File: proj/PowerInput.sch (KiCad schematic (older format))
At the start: 23 parts, among them Q1 MMBT3906, Q2 IRLML6402, U1 TL431AIDBZ, U2 LM393M

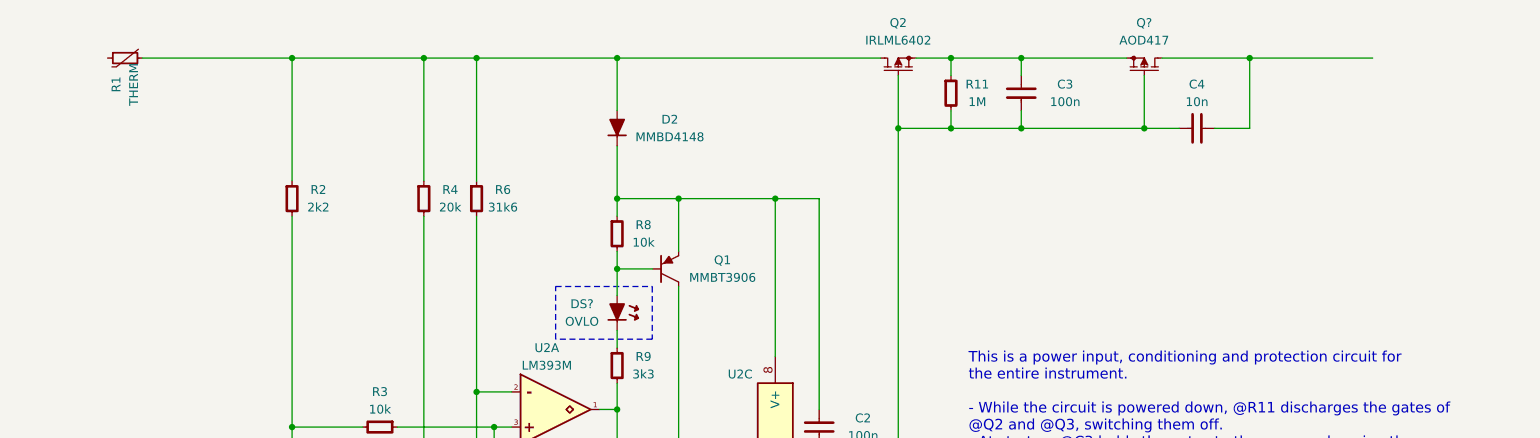
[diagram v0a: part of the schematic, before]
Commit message: Add DC-DC
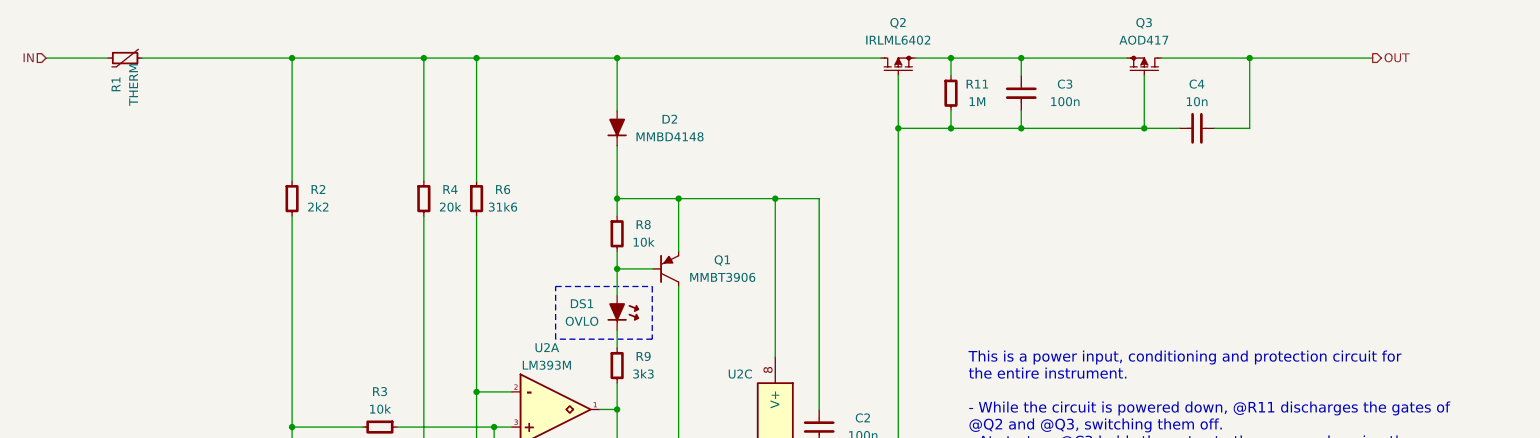
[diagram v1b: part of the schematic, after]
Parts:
- gave numbers to parts that had none: 2
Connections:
- net IN: now reaches R1.1
- net OUT: now reaches C4.1, Q3.3 (D)
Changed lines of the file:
@@
 $Descr USLegal 14000 8500
 encoding utf-8
-Sheet 3 13
+Sheet 3 14
 Title ""
 Date ""
@@
 Connection ~ 4450 5100
 $Comp
-L GND #PWR1
+L GND #PWR2
 U 1 1 54F4C586
 P 4450 6050
-F 0 "#PWR1" H 4450 6050 30  0001 C CNN
+F 0 "#PWR2" H 4450 6050 30  0001 C CNN
 F 1 "GND" H 4450 5980 30  0001 C CNN
 F 2 "" H 4450 6050 60  0000 C CNN
@@
 $EndComp
 $Comp
-L GND #PWR2
+L GND #PWR3
 U 1 1 54F4C600
 P 5200 6000
-F 0 "#PWR2" H 5200 6000 30  0001 C CNN
+F 0 "#PWR3" H 5200 6000 30  0001 C CNN
 F 1 "GND" H 5200 5930 30  0001 C CNN
 F 2 "" H 5200 6000 60  0000 C CNN
@@
 	5200 6000 5200 5900
 $Comp
-L GND #PWR3
+L GND #PWR4
 U 1 1 54F4C674
 P 5500 6000
-F 0 "#PWR3" H 5500 6000 30  0001 C CNN
+F 0 "#PWR4" H 5500 6000 30  0001 C CNN
 F 1 "GND" H 5500 5930 30  0001 C CNN
 F 2 "" H 5500 6000 60  0000 C CNN
@@
 Connection ~ 7200 2900
 $Comp
-L GND #PWR6
+L GND #PWR7
 U 1 1 54F4D4FF
 P 7450 4400
-F 0 "#PWR6" H 7450 4400 30  0001 C CNN
+F 0 "#PWR7" H 7450 4400 30  0001 C CNN
 F 1 "GND" H 7450 4330 30  0001 C CNN
 F 2 "" H 7450 4400 60  0000 C CNN
@@
 	7450 4400 7450 4300
 $Comp
-L GND #PWR5
+L GND #PWR6
 U 1 1 54F4D5D3
 P 7200 4700
-F 0 "#PWR5" H 7200 4700 30  0001 C CNN
+F 0 "#PWR6" H 7200 4700 30  0001 C CNN
 F 1 "GND" H 7200 4630 30  0001 C CNN
 F 2 "" H 7200 4700 60  0000 C CNN
@@
 Connection ~ 5500 5600
 $Comp
-L GND #PWR4
+L GND #PWR5
 U 1 1 54F4E909
 P 5850 6000
-F 0 "#PWR4" H 5850 6000 30  0001 C CNN
+F 0 "#PWR5" H 5850 6000 30  0001 C CNN
 F 1 "GND" H 5850 5930 30  0001 C CNN
 F 2 "" H 5850 6000 60  0000 C CNN
@@
 $EndComp
 $Comp
-L AOD417 Q?
+L AOD417 Q3
 U 1 1 54F5B784
 P 9300 2150
-F 0 "Q?" V 9550 2150 50  0000 C CNN
+F 0 "Q3" V 9550 2150 50  0000 C CNN
 F 1 "AOD417" V 9450 2150 50  0000 C CNN
 F 2 "smd-semi:TO-252" H 9450 2100 50  0001 C CNN
@@
 $EndComp
 $Comp
-L LED-0603 DS?
+L LED-0603 DS1
 U 1 1 54F5C5AB
 P 6300 3550
-F 0 "DS?" H 6100 3600 50  0000 C CNN
+F 0 "DS1" H 6100 3600 50  0000 C CNN
 F 1 "OVLO" H 6100 3500 50  0000 C CNN
 F 2 "smd-semi:LED-0603" H 6300 3550 50  0001 C CNN
@@
 	1    0    0    -1
 $EndComp
+Text HLabel 10600 2100 2    50   Output ~ 0
+OUT
+Text HLabel 3050 2100 0    50   Input ~ 0
+IN
+Wire Wire Line
+	3050 2100 3400 2100
 $EndSCHEMATC

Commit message: Finish USB subcircuit
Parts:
- added Q?: MMBT3904, smd-semi:SOT-23, symbol MMBT3904
- added R? (x2): 10k, IPC7351-Nominal:RESC1005X40, symbol R-0402
- R1: value THERM -> 350mA; footprint (none) -> IPC7351-Nominal:RESC3216X60; BOM (none) -> DIST DIGIKEY 507-1801-1-ND; Manuf (none) -> BelFuse; PN (none) -> 0ZCJ0035AF2E
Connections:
- net GND: now also Q?.2, R?.2
- net at R4.2, R5.1, U2.6: now also Q?.3
- new net: Q?.1, R?.1, R?.1
- new net PWRDN: R?.2
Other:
- moved on the sheet: C2, C3, C4, Q2, Q3, R11, R2, U1, U2C

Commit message: Start PCB
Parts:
- gave numbers to parts that had none: 3
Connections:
- net GND: no longer R2.2, R3.2, U1.2, U2.5
- net at U1.1: now also R2.2, R3.2, U1.2, U2.5
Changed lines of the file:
@@
 $EndComp
 Wire Wire Line
-	3600 2100 4100 2100
-Wire Wire Line
-	4100 2100 5200 2100
-Wire Wire Line
-	5200 2100 5500 2100
-Wire Wire Line
-	5500 2100 6300 2100
-Wire Wire Line
-	6300 2100 8300 2100
-Wire Wire Line
-	8500 2100 8700 2100
-Wire Wire Line
-	8700 2100 9100 2100
-Wire Wire Line
-	9100 2100 9700 2100
-Wire Wire Line
-	8400 5000 8400 2500
-Wire Wire Line
-	8400 2500 8400 2200
-Wire Wire Line
-	8400 2500 8700 2500
-Wire Wire Line
-	8700 2500 9100 2500
-Wire Wire Line
-	9100 2500 9800 2500
-Wire Wire Line
-	9800 2500 10000 2500
+	3600 2100 8300 2100
+Wire Wire Line
+	8500 2100 9700 2100
+Wire Wire Line
+	8400 5000 8400 2200
+Wire Wire Line
+	8400 2500 10000 2500
 Wire Wire Line
 	9800 2500 9800 2200
 Wire Wire Line
-	9900 2100 10400 2100
-Wire Wire Line
-	10400 2100 11100 2100
+	9900 2100 11100 2100
 $Comp
 L R-0402 R11
@@
 $EndComp
 Wire Wire Line
-	6300 3950 6300 4100
-Wire Wire Line
-	6300 4100 6300 4500
+	6300 3950 6300 4500
 Wire Wire Line
 	6300 4100 6200 4100
@@
 $EndComp
 Wire Wire Line
-	6300 3200 6300 3300
-Wire Wire Line
-	6300 3300 6300 3450
+	6300 3200 6300 3450
 $Comp
 L MMBT3906 Q1
@@
 	6650 3400 6650 5000
 Wire Wire Line
-	6550 5000 6650 5000
-Wire Wire Line
-	6650 5000 8400 5000
+	6550 5000 8400 5000
 Wire Wire Line
 	6650 3200 6650 2900
 Wire Wire Line
-	6300 2600 6300 2900
-Wire Wire Line
-	6300 2900 6300 3000
+	6300 2600 6300 3000
 $Comp
 L MMBD4148 D1
@@
 	5600 4500 5600 4200
 Wire Wire Line
-	5050 4200 5600 4200
-Wire Wire Line
-	5600 4200 5700 4200
+	5050 4200 5700 4200
 $Comp
 L R-0402 R3
@@
 $EndComp
 Wire Wire Line
-	5200 3000 5200 4900
-Wire Wire Line
-	5200 4900 5200 5300
-Wire Wire Line
-	5200 5300 5200 5700
+	5200 3000 5200 5700
 Wire Wire Line
 	5200 4900 5700 4900
@@
 $EndComp
 Wire Wire Line
-	5500 3000 5500 4000
-Wire Wire Line
-	5500 4000 5500 5600
-Wire Wire Line
-	5500 5600 5500 5700
+	5500 3000 5500 5700
 Wire Wire Line
 	5500 4000 5700 4000
@@
 	4100 5100 5700 5100
 Wire Wire Line
-	4100 3000 4100 4200
-Wire Wire Line
-	4100 4200 4100 5100
-Wire Wire Line
-	4100 5100 4100 5600
-Wire Wire Line
-	4100 5600 4100 5950
-Wire Wire Line
-	4100 5950 4100 6050
-Wire Wire Line
 	4100 4200 4850 4200
 $Comp
@@
 Connection ~ 4100 5100
 $Comp
-L GND #PWR2
+L GND #PWR0209
 U 1 1 54F4C586
 P 4100 6050
-F 0 "#PWR2" H 4100 6050 30  0001 C CNN
+F 0 "#PWR0209" H 4100 6050 30  0001 C CNN
 F 1 "GND" H 4100 5980 30  0001 C CNN
 F 2 "" H 4100 6050 60  0000 C CNN
@@
 $EndComp
 $Comp
-L GND #PWR3
+L GND #PWR0210
 U 1 1 54F4C600
 P 5200 6000
-F 0 "#PWR3" H 5200 6000 30  0001 C CNN
+F 0 "#PWR0210" H 5200 6000 30  0001 C CNN
 F 1 "GND" H 5200 5930 30  0001 C CNN
 F 2 "" H 5200 6000 60  0000 C CNN
@@
 	5200 6000 5200 5900
 $Comp
-L GND #PWR4
+L GND #PWR0211
 U 1 1 54F4C674
 P 5500 6000
-F 0 "#PWR4" H 5500 6000 30  0001 C CNN
+F 0 "#PWR0211" H 5500 6000 30  0001 C CNN
 F 1 "GND" H 5500 5930 30  0001 C CNN
 F 2 "" H 5500 6000 60  0000 C CNN
@@
 Connection ~ 7300 2900
 $Comp
-L GND #PWR7
+L GND #PWR0212
 U 1 1 54F4D4FF
 P 7550 4400
-F 0 "#PWR7" H 7550 4400 30  0001 C CNN
+F 0 "#PWR0212" H 7550 4400 30  0001 C CNN
 F 1 "GND" H 7550 4330 30  0001 C CNN
 F 2 "" H 7550 4400 60  0000 C CNN
@@
 	7550 4400 7550 4300
 $Comp
-L GND #PWR6
+L GND #PWR0213
 U 1 1 54F4D5D3
 P 7300 4700
-F 0 "#PWR6" H 7300 4700 30  0001 C CNN
+F 0 "#PWR0213" H 7300 4700 30  0001 C CNN
 F 1 "GND" H 7300 4630 30  0001 C CNN
 F 2 "" H 7300 4700 60  0000 C CNN
@@
 Connection ~ 5500 5600
 $Comp
-L GND #PWR5
+L GND #PWR0214
 U 1 1 54F4E909
 P 5850 6000
-F 0 "#PWR5" H 5850 6000 30  0001 C CNN
+F 0 "#PWR0214" H 5850 6000 30  0001 C CNN
 F 1 "GND" H 5850 5930 30  0001 C CNN
 F 2 "" H 5850 6000 60  0000 C CNN
@@
 Wire Notes Line
 	5950 3700 5950 3400
-Connection ~ 4100 5950
 $Comp
 L IRLML6402 Q2
@@
 	3050 2100 3400 2100
 $Comp
-L MMBT3904 Q?
+L MMBT3904 Q14
 U 1 1 54F7D19E
 P 4950 6300
-F 0 "Q?" H 5100 6300 50  0000 C CNN
+F 0 "Q14" H 5100 6300 50  0000 C CNN
 F 1 "MMBT3904" H 5250 6250 50  0001 C CNN
 F 2 "smd-semi:SOT-23" H 4950 6300 50  0001 C CNN
@@
 	5000 5300 5000 6200
 $Comp
-L GND #PWR?
+L GND #PWR0215
 U 1 1 54F7D2C2
 P 5000 6450
-F 0 "#PWR?" H 5000 6450 30  0001 C CNN
+F 0 "#PWR0215" H 5000 6450 30  0001 C CNN
 F 1 "GND" H 5000 6380 30  0001 C CNN
 F 2 "" H 5000 6450 60  0000 C CNN
@@
 	5000 6450 5000 6400
 $Comp
-L R-0402 R?
+L R-0402 R91
 U 1 1 54F7D463
 P 4750 6800
-F 0 "R?" H 4900 6850 50  0000 C CNN
+F 0 "R91" H 4900 6850 50  0000 C CNN
 F 1 "10k" H 4900 6750 50  0000 C CNN
 F 2 "IPC7351-Nominal:RESC1005X40" H 4750 6800 50  0001 C CNN
@@
 $EndComp
 Wire Wire Line
-	4750 6300 4750 6600
-Wire Wire Line
-	4750 6600 4750 6700
+	4750 6300 4750 6700
 Wire Wire Line
 	4750 6300 4850 6300
 $Comp
-L GND #PWR?
+L GND #PWR0216
 U 1 1 54F7D63A
 P 4750 7000
-F 0 "#PWR?" H 4750 7000 30  0001 C CNN
+F 0 "#PWR0216" H 4750 7000 30  0001 C CNN
 F 1 "GND" H 4750 6930 30  0001 C CNN
 F 2 "" H 4750 7000 60  0000 C CNN
@@
 	4750 7000 4750 6900
 $Comp
-L R-0402 R?
+L R-0402 R90
 U 1 1 54F7D8F0
 P 4450 6600
-F 0 "R?" V 4250 6600 50  0000 C CNN
+F 0 "R90" V 4250 6600 50  0000 C CNN
 F 1 "10k" V 4350 6600 50  0000 C CNN
 F 2 "IPC7351-Nominal:RESC1005X40" H 4450 6600 50  0001 C CNN
@@
 	4150 6600 4350 6600
 Wire Wire Line
-	6300 2900 6650 2900
-Wire Wire Line
-	6650 2900 7300 2900
-Wire Wire Line
-	7300 2900 7550 2900
+	6300 2900 7550 2900
 Wire Wire Line
 	5000 5300 5200 5300
 Connection ~ 5200 5300
+Wire Wire Line
+	4100 5950 4100 6050
+Wire Wire Line
+	4100 5650 4100 3000
 $EndSCHEMATC

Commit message: Lots of layout work
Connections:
- net at D1.3, R9.2: now also U2.7; no longer U2.1
- net at C1.2, R6.2, R7.1: now also U2.6; no longer U2.2
- net at D1.1, R3.1: now also U2.5; no longer U2.3
- net at R2.2, R3.2, U1.1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: now also U2.3; no longer U2.5
- net at Q14.3, R4.2, R5.1: now also U2.2; no longer U2.6
- net at R10.2: now also U2.1; no longer U2.7
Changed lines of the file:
@@
 $Comp
 L LM393M U2
-U 1 1 54F4B46C
+U 2 1 54F4B46C
 P 5900 4100
 F 0 "U2" H 5900 4450 50  0000 C CNN
@@
 F 2 "IPC7351-Nominal:SOIC127P600X175-8" H 5900 4100 50  0001 C CNN
 F 3 "" V 5900 4250 60  0000 C CNN
-	1    5900 4100
+	2    5900 4100
 	1    0    0    -1
 $EndComp
@@
 $Comp
 L LM393M U2
-U 2 1 54F4BA7F
+U 1 1 54F4BA7F
 P 5900 5000
 F 0 "U2" H 5900 5350 50  0000 C CNN
@@
 F 2 "IPC7351-Nominal:SOIC127P600X175-8" H 5900 5000 50  0001 C CNN
 F 3 "" V 5900 5150 60  0000 C CNN
-	2    5900 5000
+	1    5900 5000
 	1    0    0    -1
 $EndComp
@@
 Connection ~ 4100 5100
 $Comp
-L GND #PWR0237
+L GND #PWR0244
 U 1 1 54F4C586
 P 4100 6050
-F 0 "#PWR0237" H 4100 6050 30  0001 C CNN
+F 0 "#PWR0244" H 4100 6050 30  0001 C CNN
 F 1 "GND" H 4100 5980 30  0001 C CNN
 F 2 "" H 4100 6050 60  0000 C CNN
@@
 $EndComp
 $Comp
-L GND #PWR0238
+L GND #PWR0245
 U 1 1 54F4C600
 P 5200 6000
-F 0 "#PWR0238" H 5200 6000 30  0001 C CNN
+F 0 "#PWR0245" H 5200 6000 30  0001 C CNN
 F 1 "GND" H 5200 5930 30  0001 C CNN
 F 2 "" H 5200 6000 60  0000 C CNN
@@
 	5200 6000 5200 5900
 $Comp
-L GND #PWR0239
+L GND #PWR0246
 U 1 1 54F4C674
 P 5500 6000
-F 0 "#PWR0239" H 5500 6000 30  0001 C CNN
+F 0 "#PWR0246" H 5500 6000 30  0001 C CNN
 F 1 "GND" H 5500 5930 30  0001 C CNN
 F 2 "" H 5500 6000 60  0000 C CNN
@@
 Connection ~ 7300 2900
 $Comp
-L GND #PWR0240
+L GND #PWR0247
 U 1 1 54F4D4FF
 P 7550 4400
-F 0 "#PWR0240" H 7550 4400 30  0001 C CNN
+F 0 "#PWR0247" H 7550 4400 30  0001 C CNN
 F 1 "GND" H 7550 4330 30  0001 C CNN
 F 2 "" H 7550 4400 60  0000 C CNN
@@
 	7550 4400 7550 4300
 $Comp
-L GND #PWR0241
+L GND #PWR0248
 U 1 1 54F4D5D3
 P 7300 4700
-F 0 "#PWR0241" H 7300 4700 30  0001 C CNN
+F 0 "#PWR0248" H 7300 4700 30  0001 C CNN
 F 1 "GND" H 7300 4630 30  0001 C CNN
 F 2 "" H 7300 4700 60  0000 C CNN
@@
 Connection ~ 5500 5600
 $Comp
-L GND #PWR0242
+L GND #PWR0249
 U 1 1 54F4E909
 P 5850 6000
-F 0 "#PWR0242" H 5850 6000 30  0001 C CNN
+F 0 "#PWR0249" H 5850 6000 30  0001 C CNN
 F 1 "GND" H 5850 5930 30  0001 C CNN
 F 2 "" H 5850 6000 60  0000 C CNN
@@
 	5000 5300 5000 6200
 $Comp
-L GND #PWR0243
+L GND #PWR0250
 U 1 1 54F7D2C2
 P 5000 6450
-F 0 "#PWR0243" H 5000 6450 30  0001 C CNN
+F 0 "#PWR0250" H 5000 6450 30  0001 C CNN
 F 1 "GND" H 5000 6380 30  0001 C CNN
 F 2 "" H 5000 6450 60  0000 C CNN
@@
 	4750 6300 4850 6300
 $Comp
-L GND #PWR0244
+L GND #PWR0251
 U 1 1 54F7D63A
 P 4750 7000
-F 0 "#PWR0244" H 4750 7000 30  0001 C CNN
+F 0 "#PWR0251" H 4750 7000 30  0001 C CNN
 F 1 "GND" H 4750 6930 30  0001 C CNN
 F 2 "" H 4750 7000 60  0000 C CNN
